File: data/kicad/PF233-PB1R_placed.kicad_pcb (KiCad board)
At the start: 4 copper layers, 70 x 70 mm, 42 parts, among them M12 12 V 1.0 A switching module, Q1A 650V SJ 95mR, Q1B 650V SJ 95mR, U1 TC4420, U3 LM393

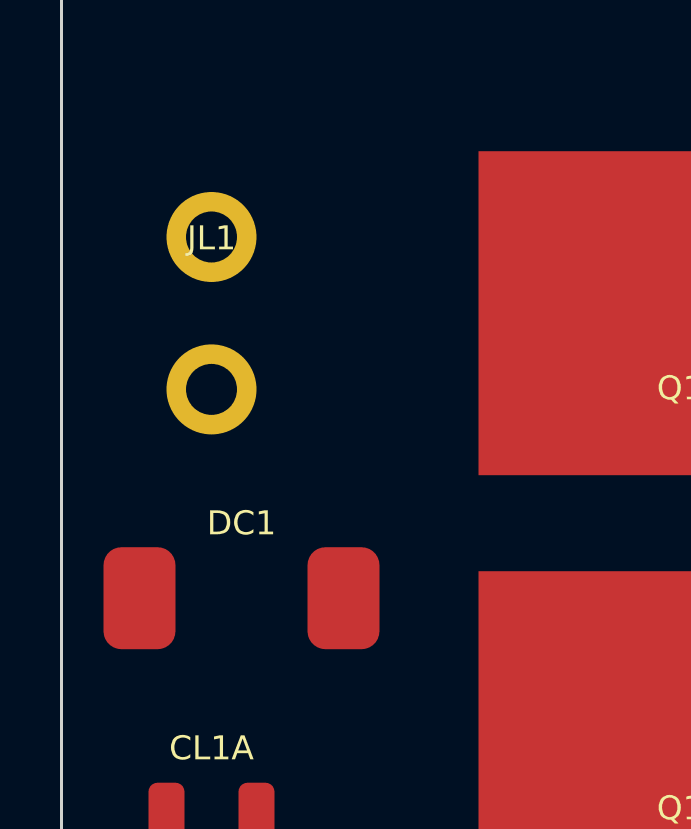
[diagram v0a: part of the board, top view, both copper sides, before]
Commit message: WIP (NOT signed off): data published by the second close-out run (8 FAIL: 3 opens on CB1D-C2 / AU1 under the exact fine-zone keep-out); third run in progress
Co-Authored-By: Claude Opus 5.5 <noreply@anthropic.com>
Claude-Session: https://claude.ai/code/session_01FX4DWSYYjMCFGGA6gmha65
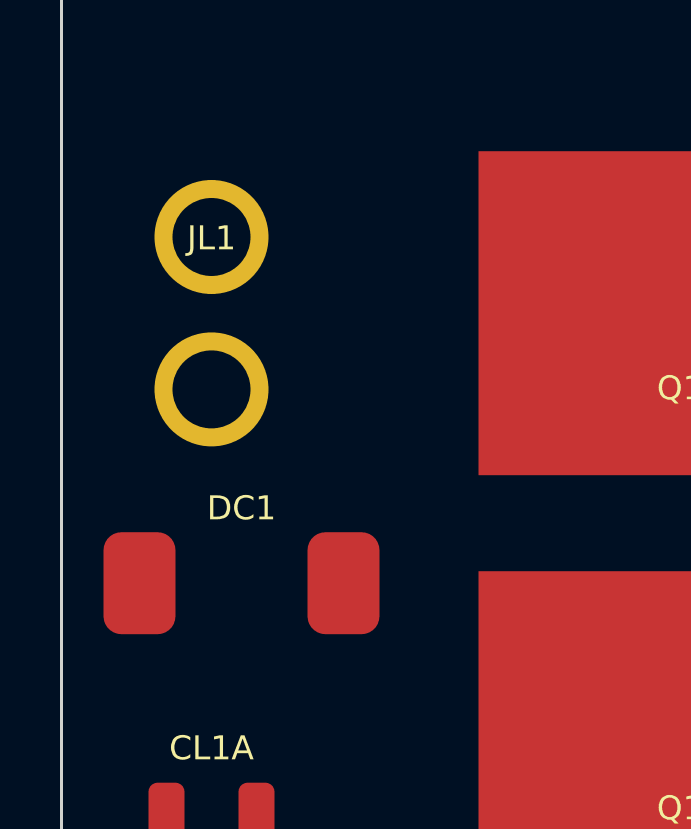
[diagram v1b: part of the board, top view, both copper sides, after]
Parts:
- JL1: value Coil outer band: DRAIN, VBUS -> Coil pair: DRAIN1, VBUS (AWG12 soldered); footprint Connector:Terminal_block_1x2_P5.08mm -> Connector:Solder_holes_AWG12_1x2_P5.08mm
- moved DC1 0.50 mm to (71.0, 89.0)
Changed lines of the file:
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@@
     (property "Value" "Power in: VBUS VBUS GND GND" (at 0 2.5 0) (layer "F.Fab") (effects (font (size 0.8 0.8) (thickness 0.12))))
     (attr through_hole)
-    (model "${KIPRJMOD}/3dmodels/PF233_TERM4.wrl" (offset (xyz 0 0 0)) (scale (xyz 0.3937 0.3937 0.3937)) (rotate (xyz 0 0 0)))
     (pad "1" thru_hole circle (at 0.000 -7.620) (size 3.0 3.0) (drill 1.7) (layers "*.Cu" "*.Mask") (net 19 "VBUS"))
     (pad "2" thru_hole circle (at 0.000 -2.540) (size 3.0 3.0) (drill 1.7) (layers "*.Cu" "*.Mask") (net 19 "VBUS"))
@@
     (property "Value" "Umbilical from the head: SHLD GND TX1_IN REF_I1 FAULT1_N ISENSE1 NTC GND" (at 0 2.5 0) (layer "F.Fab") (effects (font (size 0.8 0.8) (thickness 0.12))))
     (attr through_hole)
-    (model "${KIPRJMOD}/3dmodels/PF233_HDR2x4.wrl" (offset (xyz 0 0 0)) (scale (xyz 0.3937 0.3937 0.3937)) (rotate (xyz 0 0 0)))
     (pad "1" thru_hole circle (at -1.270 -3.810) (size 1.8 1.8) (drill 1.0) (layers "*.Cu" "*.Mask") (net 18 "UMB_SHLD"))
     (pad "2" thru_hole circle (at 1.270 -3.810) (size 1.8 1.8) (drill 1.0) (layers "*.Cu" "*.Mask") (net 10 "GND"))
@@
     (pad "2" smd roundrect (at 3.100 0.000) (size 1.600 3.400) (layers "F.Cu" "F.Paste" "F.Mask") (net 10 "GND"))
   )
-  (footprint "Diode_SMD:D_SMC" (layer "F.Cu") (at 71.0000 89.5000)
+  (footprint "Diode_SMD:D_SMC" (layer "F.Cu") (at 71.0000 89.0000)
     (property "Reference" "DC1" (at 0 -2.5 0) (layer "F.SilkS") (effects (font (size 0.8 0.8) (thickness 0.12))))
     (property "Value" "ES3J 600V 3A" (at 0 2.5 0) (layer "F.Fab") (effects (font (size 0.8 0.8) (thickness 0.12))))
@@
     (pad "2" thru_hole circle (at 2.540 0.000) (size 3.0 3.0) (drill 1.6) (layers "*.Cu" "*.Mask") (net 19 "VBUS"))
   )
-  (footprint "Connector:Terminal_block_1x2_P5.08mm" (layer "F.Cu") (at 70.0000 80.0000)
+  (footprint "Connector:Solder_holes_AWG12_1x2_P5.08mm" (layer "F.Cu") (at 70.0000 80.0000)
     (property "Reference" "JL1" (at 0 -2.5 0) (layer "F.SilkS") (effects (font (size 0.8 0.8) (thickness 0.12))))
-    (property "Value" "Coil outer band: DRAIN, VBUS" (at 0 2.5 0) (layer "F.Fab") (effects (font (size 0.8 0.8) (thickness 0.12))))
-    (attr through_hole)
-    (model "${KIPRJMOD}/3dmodels/PF233_TERM2.wrl" (offset (xyz 0 0 0)) (scale (xyz 0.3937 0.3937 0.3937)) (rotate (xyz 0 0 0)))
-    (pad "1" thru_hole circle (at 0.000 -2.540) (size 3.0 3.0) (drill 1.7) (layers "*.Cu" "*.Mask") (net 3 "DRAIN1"))
-    (pad "2" thru_hole circle (at 0.000 2.540) (size 3.0 3.0) (drill 1.7) (layers "*.Cu" "*.Mask") (net 19 "VBUS"))
+    (property "Value" "Coil pair: DRAIN1, VBUS (AWG12 soldered)" (at 0 2.5 0) (layer "F.Fab") (effects (font (size 0.8 0.8) (thickness 0.12))))
+    (attr through_hole)
+    (pad "1" thru_hole circle (at 0.000 -2.540) (size 3.8 3.8) (drill 2.6) (layers "*.Cu" "*.Mask") (net 3 "DRAIN1"))
+    (pad "2" thru_hole circle (at 0.000 2.540) (size 3.8 3.8) (drill 2.6) (layers "*.Cu" "*.Mask") (net 19 "VBUS"))
   )
   (footprint "Resistor_SMD:R_0603_1608Metric" (layer "F.Cu") (at 98.5000 106.8000)

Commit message: Close-out of the output modes / audio / gyro integration: sign-off 76 PASS / 0 FAIL / 4 UNVERIFIED, strict regress 114 / 0, release controls 12 / 12, publish 0 stale
AU1 (36 x 60, 8 layers, gyro moved from CB1D) routed 38 / 38, CB1D-C2 46 / 46, both exact DRC 0 / 0; PB1R-v5 AWG12 solder holes; PM2-B, HB2-B; superseded Gerber sets marked.
Tooling now default: exact-geometry DRC, router fine-pitch keep-out / neck-down / per-board grid, local repair, round checkpoints, non-destructive reset,
interface check, AU1 3-D models with gull-wing leads, counted HV check; pad check traced by the pipeline; process-guard regress row; PROCESS.md / CLAUDE.md / handoff updated.

Co-Authored-By: Claude Opus 5.5 <noreply@anthropic.com>
Claude-Session: https://claude.ai/code/session_01FX4DWSYYjMCFGGA6gmha65
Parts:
- removed the JC at (128.0, 124.0)
- removed the JP at (70.0, 124.0)
- added JC: Umbilical from the head: SHLD GND TX1_IN REF_I1 FAULT1_N IS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, Connector:Wire_pads_2x4_P2.54mm, F.Cu at (128.0, 124.0)
- added JP: Power in: VBUS VBUS GND GND, Connector:Wire_pads_1x4_P5.08mm, F.Cu at (70.0, 124.0)
- JL1: footprint Connector:Solder_holes_AWG12_1x2_P5.08mm -> Connector:Wire_pads_AWG12_1x2_P5.08mm
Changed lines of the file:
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@@
   (net 18 "UMB_SHLD")
   (net 19 "VBUS")
-  (footprint "Connector:Terminal_block_1x4_P5.08mm" (layer "F.Cu") (at 70.0000 124.0000)
+  (footprint "Connector:Wire_pads_1x4_P5.08mm" (layer "F.Cu") (at 70.0000 124.0000)
     (property "Reference" "JP" (at 0 -2.5 0) (layer "F.SilkS") (effects (font (size 0.8 0.8) (thickness 0.12))))
     (property "Value" "Power in: VBUS VBUS GND GND" (at 0 2.5 0) (layer "F.Fab") (effects (font (size 0.8 0.8) (thickness 0.12))))
@@
     (pad "2" smd roundrect (at 1.500 0.000) (size 1.200 2.700) (layers "F.Cu" "F.Paste" "F.Mask") (net 10 "GND"))
   )
-  (footprint "Connector:Pin_header_2x4_P2.54mm" (layer "F.Cu") (at 128.0000 124.0000)
+  (footprint "Connector:Wire_pads_2x4_P2.54mm" (layer "F.Cu") (at 128.0000 124.0000)
     (property "Reference" "JC" (at 0 -2.5 0) (layer "F.SilkS") (effects (font (size 0.8 0.8) (thickness 0.12))))
     (property "Value" "Umbilical from the head: SHLD GND TX1_IN REF_I1 FAULT1_N ISENSE1 NTC GND" (at 0 2.5 0) (layer "F.Fab") (effects (font (size 0.8 0.8) (thickness 0.12))))
@@
     (pad "2" thru_hole circle (at 2.540 0.000) (size 3.0 3.0) (drill 1.6) (layers "*.Cu" "*.Mask") (net 19 "VBUS"))
   )
-  (footprint "Connector:Solder_holes_AWG12_1x2_P5.08mm" (layer "F.Cu") (at 70.0000 80.0000)
+  (footprint "Connector:Wire_pads_AWG12_1x2_P5.08mm" (layer "F.Cu") (at 70.0000 80.0000)
     (property "Reference" "JL1" (at 0 -2.5 0) (layer "F.SilkS") (effects (font (size 0.8 0.8) (thickness 0.12))))
     (property "Value" "Coil pair: DRAIN1, VBUS (AWG12 soldered)" (at 0 2.5 0) (layer "F.Fab") (effects (font (size 0.8 0.8) (thickness 0.12))))

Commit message: WIP: published PB1R KiCad / schematic outputs and pipeline graph for the B7 close-out (sign-off re-run pending)
Co-Authored-By: Claude Opus 5.5 <noreply@anthropic.com>
Claude-Session: https://claude.ai/code/session_01FX4DWSYYjMCFGGA6gmha65
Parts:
- RCL1: value external 5k 10W (lid bank) -> 4 x Vishay PR03 1K24 1% 750V 3W in series, 4.96k, NPM hot zone
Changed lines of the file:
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@@
   (footprint "Connector:SolderPad_2x_P5.08mm" (layer "F.Cu") (at 71.0000 109.5000)
     (property "Reference" "RCL1" (at 0 -2.5 0) (layer "F.SilkS") (effects (font (size 0.8 0.8) (thickness 0.12))))
-    (property "Value" "external 5k 10W (lid bank)" (at 0 2.5 0) (layer "F.Fab") (effects (font (size 0.8 0.8) (thickness 0.12))))
+    (property "Value" "4 x Vishay PR03 1K24 1% 750V 3W in series, 4.96k, NPM hot zone" (at 0 2.5 0) (layer "F.Fab") (effects (font (size 0.8 0.8) (thickness 0.12))))
     (attr through_hole)
     (pad "1" thru_hole circle (at -2.540 0.000) (size 3.0 3.0) (drill 1.6) (layers "*.Cu" "*.Mask") (net 2 "CLAMP1"))

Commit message: Speed-up: batched Gerber geometry (10x, same copper) and parallel sign-off controls (245 s -> 32 s); B7 sign-off run
gerber_geom.layer_geometry merges same-polarity runs with unary_union (worst sym-diff 6e-13 mm2
over 258 layers; regress row keeps the sequential build as reference). publish 79 -> 10.5 s.
release_signoff_controls runs independent jobs in a thread pool, stale-data control alone last.
Sign-off 77 PASS / 0 FAIL / 3 UNVERIFIED, strict regress 120 / 0, publish 0 stale.
Moved: US3M diode margins (reverse voltage 27.5 -> 56.5 %, current 80.1 -> 83.4 %).

Co-Authored-By: Claude Opus 5.5 <noreply@anthropic.com>
Claude-Session: https://claude.ai/code/session_01FX4DWSYYjMCFGGA6gmha65
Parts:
- DC1: value ES3J 600V 3A -> US3M 1000V 3A
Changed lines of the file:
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@@
   (footprint "Diode_SMD:D_SMC" (layer "F.Cu") (at 71.0000 89.0000)
     (property "Reference" "DC1" (at 0 -2.5 0) (layer "F.SilkS") (effects (font (size 0.8 0.8) (thickness 0.12))))
-    (property "Value" "ES3J 600V 3A" (at 0 2.5 0) (layer "F.Fab") (effects (font (size 0.8 0.8) (thickness 0.12))))
+    (property "Value" "US3M 1000V 3A" (at 0 2.5 0) (layer "F.Fab") (effects (font (size 0.8 0.8) (thickness 0.12))))
     (attr smd)
     (model "${KIPRJMOD}/3dmodels/PF233_DSMC.wrl" (offset (xyz 0 0 0)) (scale (xyz 0.3937 0.3937 0.3937)) (rotate (xyz 0 0 0)))
